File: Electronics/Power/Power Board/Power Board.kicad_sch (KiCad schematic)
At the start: 1 part

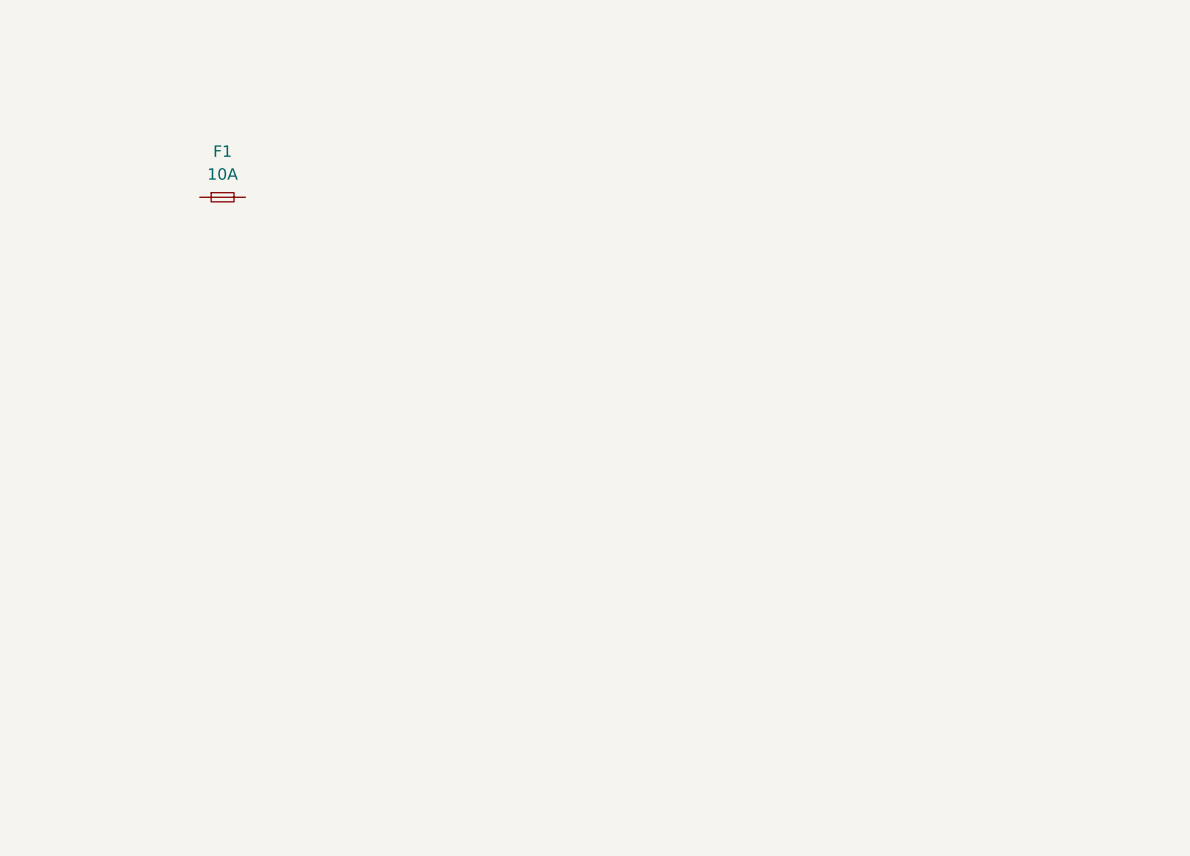
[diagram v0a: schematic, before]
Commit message: Created power board and firmware projects
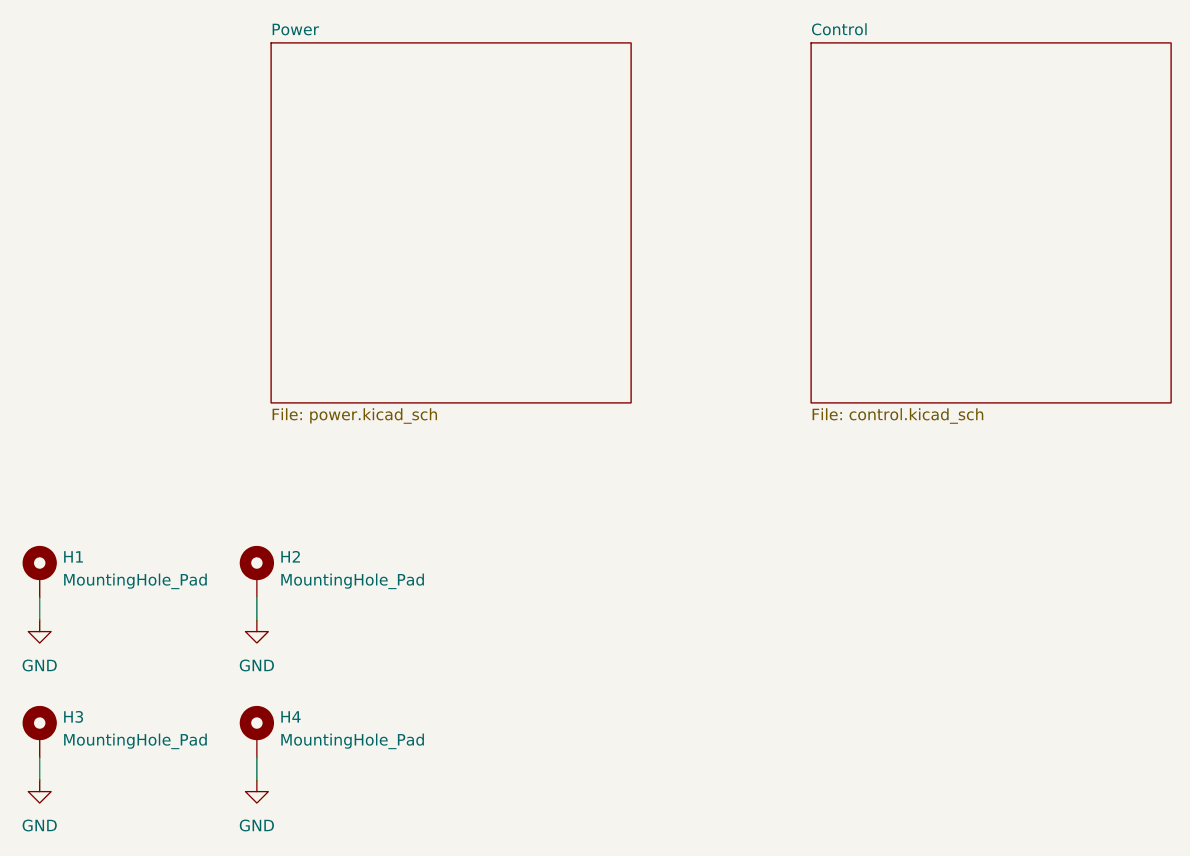
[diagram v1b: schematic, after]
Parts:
- removed F1: 10A, Fuse:Fuseholder_Cylinder-5x20mm_Schurter_0031_8201_Horizontal_Open, symbol Device:Fuse_Small
- added H1, H2, H3, H4: MountingHole_Pad, MountingHole:MountingHole_3.2mm_M3_DIN965_Pad, symbol Mechanical:MountingHole_Pad
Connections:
- new net GND: H1.1, H2.1, H3.1, H4.1
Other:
- added sheet Control (control.kicad_sch)
- added sheet Power (power.kicad_sch)
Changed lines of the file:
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@@
 (kicad_sch (version 20230121) (generator eeschema)
-  (paper "A4")
-  (symbol (lib_id "Device:Fuse_Small") (at 54.61 57.15 0) (unit 1)
-    (in_bom yes) (on_board yes) (dnp no)
-    (property "Reference" "F1" (at 54.61 52.07 0)
-      (effects (font (size 1.27 1.27)))
-    )
-    (property "Value" "10A" (at 54.61 54.61 0)
-      (effects (font (size 1.27 1.27)))
-    )
-    (property "Footprint" "Fuse:Fuseholder_Cylinder-5x20mm_Schurter_0031_8201_Horizontal_Open" (at 54.61 57.15 0)
-      (effects (font (size 1.27 1.27)) hide)
-    )
-    (property "Datasheet" "~" (at 54.61 57.15 0)
-      (effects (font (size 1.27 1.27)) hide)
-    )
-    (pin "1")
-    (pin "2")
-    (instances
-      (project "Power Board"
-        (path "/d8843e0a-fd8a-4193-ba57-f0164156e030"
-          (reference "F1") (unit 1)
-        )
-      )
-    )
+  (paper "A5")
+  (wire (pts (xy 34.29 104.14) (xy 34.29 101.6))
+    (stroke (width 0) (type default))
+  )
+  (wire (pts (xy 58.42 104.14) (xy 58.42 101.6))
+    (stroke (width 0) (type default))
+  )
+  (wire (pts (xy 34.29 121.92) (xy 34.29 119.38))
+    (stroke (width 0) (type default))
+  )
+  (wire (pts (xy 58.42 121.92) (xy 58.42 119.38))
+    (stroke (width 0) (type default))
+  )
+  (symbol (lib_id "power:GND") (at 34.29 121.92 0) (unit 1)
+    (in_bom yes) (on_board yes) (dnp no) (fields_autoplaced)
+    (property "Reference" "#PWR03" (at 34.29 128.27 0)
+      (effects (font (size 1.27 1.27)) hide)
+    )
+    (property "Value" "GND" (at 34.29 127 0)
+      (effects (font (size 1.27 1.27)))
+    )
+    (property "Footprint" "" (at 34.29 121.92 0)
+      (effects (font (size 1.27 1.27)) hide)
+    )
+    (property "Datasheet" "" (at 34.29 121.92 0)
+      (effects (font (size 1.27 1.27)) hide)
+    )
+    (pin "1")
+    (instances
+      (project "Power Board"
+        (path "/d8843e0a-fd8a-4193-ba57-f0164156e030"
+          (reference "#PWR03") (unit 1)
+        )
+      )
+    )
+  )
+  (symbol (lib_id "Mechanical:MountingHole_Pad") (at 34.29 116.84 0) (unit 1)
+    (in_bom yes) (on_board yes) (dnp no) (fields_autoplaced)
+    (property "Reference" "H3" (at 36.83 114.935 0)
+      (effects (font (size 1.27 1.27)) (justify left))
+    )
+    (property "Value" "MountingHole_Pad" (at 36.83 117.475 0)
+      (effects (font (size 1.27 1.27)) (justify left))
+    )
+    (property "Footprint" "MountingHole:MountingHole_3.2mm_M3_DIN965_Pad" (at 34.29 116.84 0)
+      (effects (font (size 1.27 1.27)) hide)
+    )
+    (property "Datasheet" "~" (at 34.29 116.84 0)
+      (effects (font (size 1.27 1.27)) hide)
+    )
+    (pin "1")
+    (instances
+      (project "Power Board"
+        (path "/d8843e0a-fd8a-4193-ba57-f0164156e030"
+          (reference "H3") (unit 1)
+        )
+      )
+    )
+  )
+  (symbol (lib_id "Mechanical:MountingHole_Pad") (at 34.29 99.06 0) (unit 1)
+    (in_bom yes) (on_board yes) (dnp no) (fields_autoplaced)
+    (property "Reference" "H1" (at 36.83 97.155 0)
+      (effects (font (size 1.27 1.27)) (justify left))
+    )
+    (property "Value" "MountingHole_Pad" (at 36.83 99.695 0)
+      (effects (font (size 1.27 1.27)) (justify left))
+    )
+    (property "Footprint" "MountingHole:MountingHole_3.2mm_M3_DIN965_Pad" (at 34.29 99.06 0)
+      (effects (font (size 1.27 1.27)) hide)
+    )
+    (property "Datasheet" "~" (at 34.29 99.06 0)
+      (effects (font (size 1.27 1.27)) hide)
+    )
+    (pin "1")
+    (instances
+      (project "Power Board"
+        (path "/d8843e0a-fd8a-4193-ba57-f0164156e030"
+          (reference "H1") (unit 1)
+        )
+      )
+    )
+  )
+  (symbol (lib_id "power:GND") (at 58.42 121.92 0) (unit 1)
+    (in_bom yes) (on_board yes) (dnp no) (fields_autoplaced)
+    (property "Reference" "#PWR04" (at 58.42 128.27 0)
+      (effects (font (size 1.27 1.27)) hide)
+    )
+    (property "Value" "GND" (at 58.42 127 0)
+      (effects (font (size 1.27 1.27)))
+    )
+    (property "Footprint" "" (at 58.42 121.92 0)
+      (effects (font (size 1.27 1.27)) hide)
+    )
+    (property "Datasheet" "" (at 58.42 121.92 0)
+      (effects (font (size 1.27 1.27)) hide)
+    )
+    (pin "1")
+    (instances
+      (project "Power Board"
+        (path "/d8843e0a-fd8a-4193-ba57-f0164156e030"
+          (reference "#PWR04") (unit 1)
+        )
+      )
+    )
+  )
+  (symbol (lib_id "Mechanical:MountingHole_Pad") (at 58.42 116.84 0) (unit 1)
+    (in_bom yes) (on_board yes) (dnp no) (fields_autoplaced)
+    (property "Reference" "H4" (at 60.96 114.935 0)
+      (effects (font (size 1.27 1.27)) (justify left))
+    )
+    (property "Value" "MountingHole_Pad" (at 60.96 117.475 0)
+      (effects (font (size 1.27 1.27)) (justify left))
+    )
+    (property "Footprint" "MountingHole:MountingHole_3.2mm_M3_DIN965_Pad" (at 58.42 116.84 0)
+      (effects (font (size 1.27 1.27)) hide)
+    )
+    (property "Datasheet" "~" (at 58.42 116.84 0)
+      (effects (font (size 1.27 1.27)) hide)
+    )
+    (pin "1")
+    (instances
+      (project "Power Board"
+        (path "/d8843e0a-fd8a-4193-ba57-f0164156e030"
+          (reference "H4") (unit 1)
+        )
+      )
+    )
+  )
+  (symbol (lib_id "power:GND") (at 58.42 104.14 0) (unit 1)
+    (in_bom yes) (on_board yes) (dnp no) (fields_autoplaced)
+    (property "Reference" "#PWR02" (at 58.42 110.49 0)
+      (effects (font (size 1.27 1.27)) hide)
+    )
+    (property "Value" "GND" (at 58.42 109.22 0)
+      (effects (font (size 1.27 1.27)))
+    )
+    (property "Footprint" "" (at 58.42 104.14 0)
+      (effects (font (size 1.27 1.27)) hide)
+    )
+    (property "Datasheet" "" (at 58.42 104.14 0)
+      (effects (font (size 1.27 1.27)) hide)
+    )
+    (pin "1")
+    (instances
+      (project "Power Board"
+        (path "/d8843e0a-fd8a-4193-ba57-f0164156e030"
+          (reference "#PWR02") (unit 1)
+        )
+      )
+    )
+  )
+  (symbol (lib_id "power:GND") (at 34.29 104.14 0) (unit 1)
+    (in_bom yes) (on_board yes) (dnp no) (fields_autoplaced)
+    (property "Reference" "#PWR01" (at 34.29 110.49 0)
+      (effects (font (size 1.27 1.27)) hide)
+    )
+    (property "Value" "GND" (at 34.29 109.22 0)
+      (effects (font (size 1.27 1.27)))
+    )
+    (property "Footprint" "" (at 34.29 104.14 0)
+      (effects (font (size 1.27 1.27)) hide)
+    )
+    (property "Datasheet" "" (at 34.29 104.14 0)
+      (effects (font (size 1.27 1.27)) hide)
+    )
+    (pin "1")
+    (instances
+      (project "Power Board"
+        (path "/d8843e0a-fd8a-4193-ba57-f0164156e030"
+          (reference "#PWR01") (unit 1)
+        )
+      )
+    )
+  )
+  (symbol (lib_id "Mechanical:MountingHole_Pad") (at 58.42 99.06 0) (unit 1)
+    (in_bom yes) (on_board yes) (dnp no) (fields_autoplaced)
+    (property "Reference" "H2" (at 60.96 97.155 0)
+      (effects (font (size 1.27 1.27)) (justify left))
+    )
+    (property "Value" "MountingHole_Pad" (at 60.96 99.695 0)
+      (effects (font (size 1.27 1.27)) (justify left))
+    )
+    (property "Footprint" "MountingHole:MountingHole_3.2mm_M3_DIN965_Pad" (at 58.42 99.06 0)
+      (effects (font (size 1.27 1.27)) hide)
+    )
+    (property "Datasheet" "~" (at 58.42 99.06 0)
+      (effects (font (size 1.27 1.27)) hide)
+    )
+    (pin "1")
+    (instances
+      (project "Power Board"
+        (path "/d8843e0a-fd8a-4193-ba57-f0164156e030"
+          (reference "H2") (unit 1)
+        )
+      )
+    )
+  )
+  (sheet (at 120 40) (size 40 40) (fields_autoplaced)
+    (stroke (width 0.1524) (type solid))
+    (fill (color 254 210 17 1.0000))
+    (property "Sheetname" "Control" (at 120 39.2884 0)
+      (effects (font (size 1.27 1.27)) (justify left bottom))
+    )
+    (property "Sheetfile" "control.kicad_sch" (at 120 80.5846 0)
+      (effects (font (size 1.27 1.27)) (justify left top))
+    )
+    (instances
+      (project "Power Board"
+        (path "/d8843e0a-fd8a-4193-ba57-f0164156e030" (page "3"))
+      )
+    )
+  )
+  (sheet (at 60 40) (size 40 40) (fields_autoplaced)
+    (stroke (width 0.1524) (type solid))
+    (fill (color 194 0 0 1.0000))
+    (property "Sheetname" "Power" (at 60 39.2884 0)
+      (effects (font (size 1.27 1.27)) (justify left bottom))
+    )
+    (property "Sheetfile" "power.kicad_sch" (at 60 80.5846 0)
+      (effects (font (size 1.27 1.27)) (justify left top))
+    )
+    (instances
+      (project "Power Board"
+        (path "/d8843e0a-fd8a-4193-ba57-f0164156e030" (page "2"))
+      )
+    )

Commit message: Motor driver + power board progress
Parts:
- renumbered H3 to H2, H2 to H3
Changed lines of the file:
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@@
   (symbol (lib_id "power:GND") (at 34.29 121.92 0) (unit 1)
     (in_bom yes) (on_board yes) (dnp no) (fields_autoplaced)
-    (property "Reference" "#PWR03" (at 34.29 128.27 0)
+    (property "Reference" "#PWR02" (at 34.29 128.27 0)
       (effects (font (size 1.27 1.27)) hide)
     )
@@
       (project "Power Board"
         (path "/d8843e0a-fd8a-4193-ba57-f0164156e030"
-          (reference "#PWR03") (unit 1)
+          (reference "#PWR02") (unit 1)
         )
       )
@@
   (symbol (lib_id "Mechanical:MountingHole_Pad") (at 34.29 116.84 0) (unit 1)
     (in_bom yes) (on_board yes) (dnp no) (fields_autoplaced)
-    (property "Reference" "H3" (at 36.83 114.935 0)
+    (property "Reference" "H2" (at 36.83 114.935 0)
       (effects (font (size 1.27 1.27)) (justify left))
     )
@@
       (project "Power Board"
         (path "/d8843e0a-fd8a-4193-ba57-f0164156e030"
-          (reference "H3") (unit 1)
+          (reference "H2") (unit 1)
         )
       )
@@
   (symbol (lib_id "power:GND") (at 58.42 104.14 0) (unit 1)
     (in_bom yes) (on_board yes) (dnp no) (fields_autoplaced)
-    (property "Reference" "#PWR02" (at 58.42 110.49 0)
+    (property "Reference" "#PWR03" (at 58.42 110.49 0)
       (effects (font (size 1.27 1.27)) hide)
     )
@@
       (project "Power Board"
         (path "/d8843e0a-fd8a-4193-ba57-f0164156e030"
-          (reference "#PWR02") (unit 1)
+          (reference "#PWR03") (unit 1)
         )
       )
@@
   (symbol (lib_id "Mechanical:MountingHole_Pad") (at 58.42 99.06 0) (unit 1)
     (in_bom yes) (on_board yes) (dnp no) (fields_autoplaced)
-    (property "Reference" "H2" (at 60.96 97.155 0)
+    (property "Reference" "H3" (at 60.96 97.155 0)
       (effects (font (size 1.27 1.27)) (justify left))
     )
@@
       (project "Power Board"
         (path "/d8843e0a-fd8a-4193-ba57-f0164156e030"
-          (reference "H2") (unit 1)
+          (reference "H3") (unit 1)
         )
       )

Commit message: PCB Schematics finished
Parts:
- renumbered H1 to H101, H2 to H102, H3 to H103, H4 to H104
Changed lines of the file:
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@@
   (symbol (lib_id "power:GND") (at 34.29 121.92 0) (unit 1)
     (in_bom yes) (on_board yes) (dnp no) (fields_autoplaced)
-    (property "Reference" "#PWR02" (at 34.29 128.27 0)
+    (property "Reference" "#PWR0102" (at 34.29 128.27 0)
       (effects (font (size 1.27 1.27)) hide)
     )
@@
       (project "Power Board"
         (path "/d8843e0a-fd8a-4193-ba57-f0164156e030"
-          (reference "#PWR02") (unit 1)
+          (reference "#PWR0102") (unit 1)
         )
       )
@@
   (symbol (lib_id "Mechanical:MountingHole_Pad") (at 34.29 116.84 0) (unit 1)
     (in_bom yes) (on_board yes) (dnp no) (fields_autoplaced)
-    (property "Reference" "H2" (at 36.83 114.935 0)
+    (property "Reference" "H102" (at 36.83 114.935 0)
       (effects (font (size 1.27 1.27)) (justify left))
     )
@@
       (project "Power Board"
         (path "/d8843e0a-fd8a-4193-ba57-f0164156e030"
-          (reference "H2") (unit 1)
+          (reference "H102") (unit 1)
         )
       )
@@
   (symbol (lib_id "Mechanical:MountingHole_Pad") (at 34.29 99.06 0) (unit 1)
     (in_bom yes) (on_board yes) (dnp no) (fields_autoplaced)
-    (property "Reference" "H1" (at 36.83 97.155 0)
+    (property "Reference" "H101" (at 36.83 97.155 0)
       (effects (font (size 1.27 1.27)) (justify left))
     )
@@
       (project "Power Board"
         (path "/d8843e0a-fd8a-4193-ba57-f0164156e030"
-          (reference "H1") (unit 1)
+          (reference "H101") (unit 1)
         )
       )
@@
   (symbol (lib_id "power:GND") (at 58.42 121.92 0) (unit 1)
     (in_bom yes) (on_board yes) (dnp no) (fields_autoplaced)
-    (property "Reference" "#PWR04" (at 58.42 128.27 0)
+    (property "Reference" "#PWR0104" (at 58.42 128.27 0)
       (effects (font (size 1.27 1.27)) hide)
     )
@@
       (project "Power Board"
         (path "/d8843e0a-fd8a-4193-ba57-f0164156e030"
-          (reference "#PWR04") (unit 1)
+          (reference "#PWR0104") (unit 1)
         )
       )
@@
   (symbol (lib_id "Mechanical:MountingHole_Pad") (at 58.42 116.84 0) (unit 1)
     (in_bom yes) (on_board yes) (dnp no) (fields_autoplaced)
-    (property "Reference" "H4" (at 60.96 114.935 0)
+    (property "Reference" "H104" (at 60.96 114.935 0)
       (effects (font (size 1.27 1.27)) (justify left))
     )
@@
       (project "Power Board"
         (path "/d8843e0a-fd8a-4193-ba57-f0164156e030"
-          (reference "H4") (unit 1)
+          (reference "H104") (unit 1)
         )
       )
@@
   (symbol (lib_id "power:GND") (at 58.42 104.14 0) (unit 1)
     (in_bom yes) (on_board yes) (dnp no) (fields_autoplaced)
-    (property "Reference" "#PWR03" (at 58.42 110.49 0)
+    (property "Reference" "#PWR0103" (at 58.42 110.49 0)
       (effects (font (size 1.27 1.27)) hide)
     )
@@
       (project "Power Board"
         (path "/d8843e0a-fd8a-4193-ba57-f0164156e030"
-          (reference "#PWR03") (unit 1)
+          (reference "#PWR0103") (unit 1)
         )
       )
@@
   (symbol (lib_id "power:GND") (at 34.29 104.14 0) (unit 1)
     (in_bom yes) (on_board yes) (dnp no) (fields_autoplaced)
-    (property "Reference" "#PWR01" (at 34.29 110.49 0)
+    (property "Reference" "#PWR0101" (at 34.29 110.49 0)
       (effects (font (size 1.27 1.27)) hide)
     )
@@
       (project "Power Board"
         (path "/d8843e0a-fd8a-4193-ba57-f0164156e030"
-          (reference "#PWR01") (unit 1)
+          (reference "#PWR0101") (unit 1)
         )
       )
@@
   (symbol (lib_id "Mechanical:MountingHole_Pad") (at 58.42 99.06 0) (unit 1)
     (in_bom yes) (on_board yes) (dnp no) (fields_autoplaced)
-    (property "Reference" "H3" (at 60.96 97.155 0)
+    (property "Reference" "H103" (at 60.96 97.155 0)
       (effects (font (size 1.27 1.27)) (justify left))
     )
@@
       (project "Power Board"
         (path "/d8843e0a-fd8a-4193-ba57-f0164156e030"
-          (reference "H3") (unit 1)
+          (reference "H103") (unit 1)
         )
       )

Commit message: Sensor hub board done
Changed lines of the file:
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@@
+    (stroke (width 0) (type default))
+  )
+  (wire (pts (xy 74.93 113.03) (xy 74.93 110.49))
+    (stroke (width 0) (type default))
+  )
+  (wire (pts (xy 81.28 113.03) (xy 74.93 113.03))
+    (stroke (width 0) (type default))
+  )
+  (wire (pts (xy 81.28 110.49) (xy 81.28 113.03))
     (stroke (width 0) (type default))
   )
@@
         )
       )
+    )
+  )
+  (symbol (lib_id "power:+3V3") (at 81.28 110.49 0) (unit 1)
+    (in_bom yes) (on_board yes) (dnp no) (fields_autoplaced)
+    (property "Reference" "#PWR0106" (at 81.28 114.3 0)
+      (effects (font (size 1.27 1.27)) hide)
+    )
+    (property "Value" "+3V3" (at 81.28 106.68 0)
+      (effects (font (size 1.27 1.27)))
+    )
+    (property "Footprint" "" (at 81.28 110.49 0)
+      (effects (font (size 1.27 1.27)) hide)
+    )
+    (property "Datasheet" "" (at 81.28 110.49 0)
+      (effects (font (size 1.27 1.27)) hide)
+    )
+    (pin "1")
+    (instances
+      (project "Power Board"
+        (path "/d8843e0a-fd8a-4193-ba57-f0164156e030"
+          (reference "#PWR0106") (unit 1)
+        )
+      )
+    )
+  )
+  (symbol (lib_id "power:+3.3V") (at 74.93 110.49 0) (unit 1)
+    (in_bom yes) (on_board yes) (dnp no) (fields_autoplaced)
+    (property "Reference" "#PWR0105" (at 74.93 114.3 0)
+      (effects (font (size 1.27 1.27)) hide)
+    )
+    (property "Value" "+3.3V" (at 74.93 106.68 0)
+      (effects (font (size 1.27 1.27)))
+    )
+    (property "Footprint" "" (at 74.93 110.49 0)
+      (effects (font (size 1.27 1.27)) hide)
+    )
+    (property "Datasheet" "" (at 74.93 110.49 0)
+      (effects (font (size 1.27 1.27)) hide)
+    )
+    (pin "1")
+    (instances
+      (project "Power Board"
+        (path "/d8843e0a-fd8a-4193-ba57-f0164156e030"
+          (reference "#PWR0105") (unit 1)
+        )
+      )
